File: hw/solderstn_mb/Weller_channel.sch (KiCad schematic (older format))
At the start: 40 parts, among them U1401 AD8552ARU, U1402 INA226, U1403 TPS2HB16AQ1, U1404 INA226, U1405 74LVC1G11, U1406 74LVC1G11, U1407 74LVC1G11

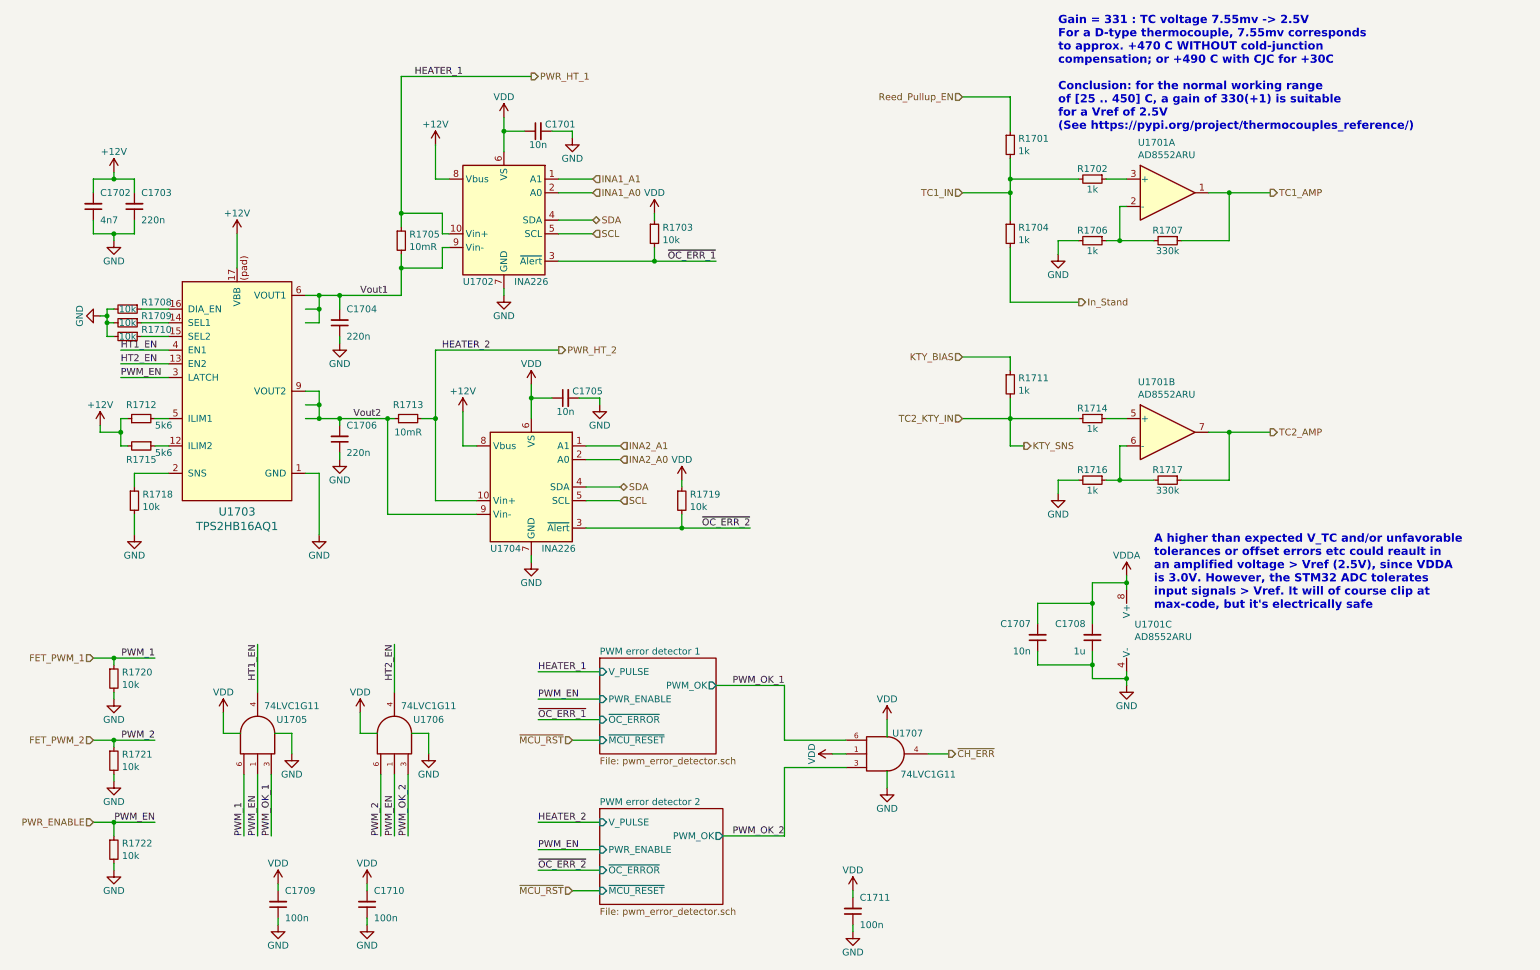
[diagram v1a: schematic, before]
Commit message: * Remove separate REED_PULLUP_EN pin; instead bias the Reedswitches with the per-channel KTY bias (buffered Vref) * Add separate mini cut-out sub-PCB for 3.5 headphone connector at back-panel (must be angled vertical to fit in panel) * Some ESD and buffering on back panel
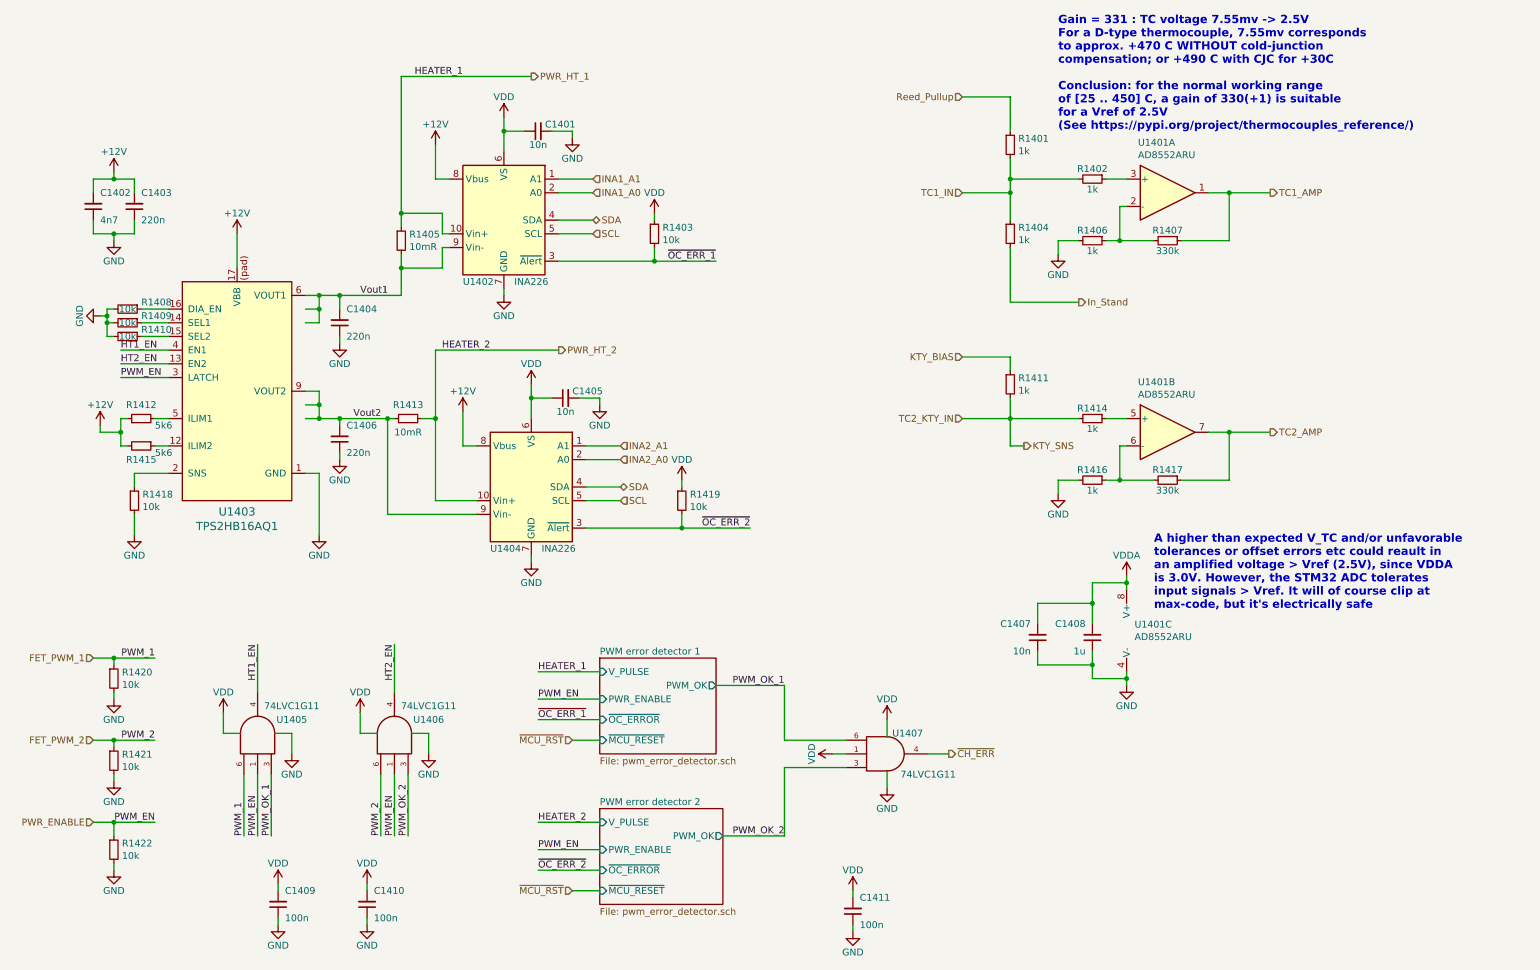
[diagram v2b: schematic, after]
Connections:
- net Reed_Pullup_EN renamed Reed_Pullup

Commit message: Updated display-board sch & PCB with optional left-hand rotary encoder instead of pwrbtn. Printed MB schematic updates PDF for 20-08-21
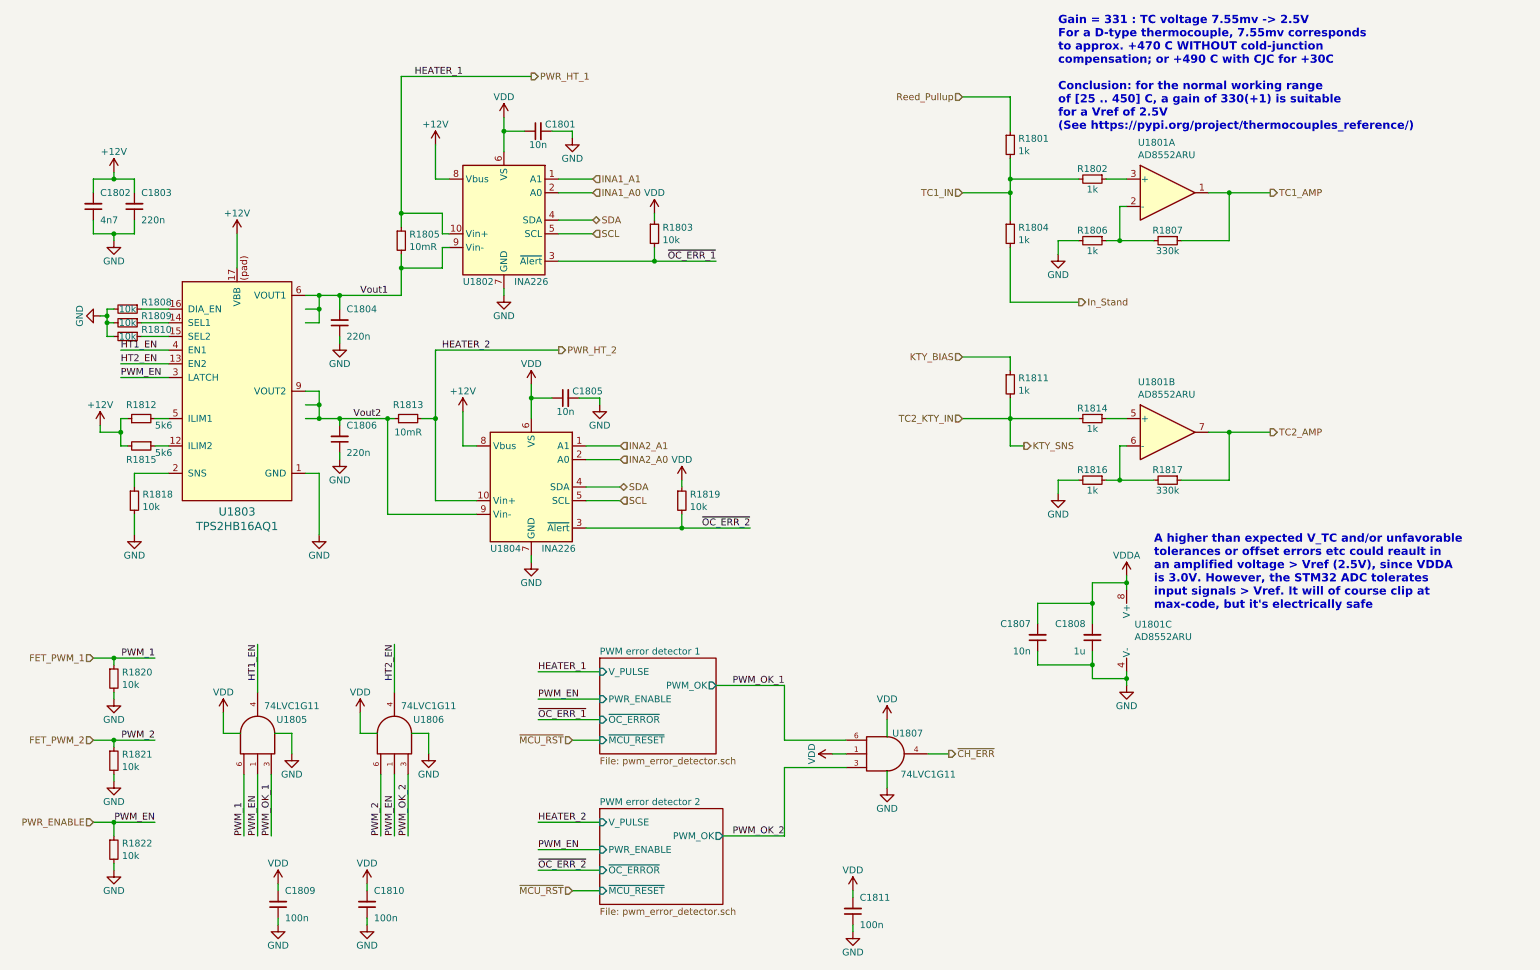
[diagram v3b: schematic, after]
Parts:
- renumbered C1401 to C1501, C1402 to C1502, C1403 to C1503, C1404 to C1504, C1405 to C1505, C1406 to C1506, C1407 to C1507, C1408 to C1508, C1409 to C1509, C1410 to C1510, C1411 to C1511, R1401 to R1501, R1402 to R1502, R1403 to R1503, R1404 to R1504, R1405 to R1505, R1406 to R1506, R1407 to R1507, R1408 to R1508, R1409 to R1509, R1410 to R1510, R1411 to R1511, R1412 to R1512, R1413 to R1513, R1414 to R1514, R1415 to R1515, R1416 to R1516, R1417 to R1517, R1418 to R1518, R1419 to R1519, R1420 to R1520, R1421 to R1521, R1422 to R1522, U1401 to U1501, U1402 to U1502, U1403 to U1503, U1404 to U1504, U1405 to U1505, U1406 to U1506, U1407 to U1507

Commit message: Corrected several ERC issues. Re-annotated & assigned all footprints except 32k xtal (will prob. replace with RTC module anyway)
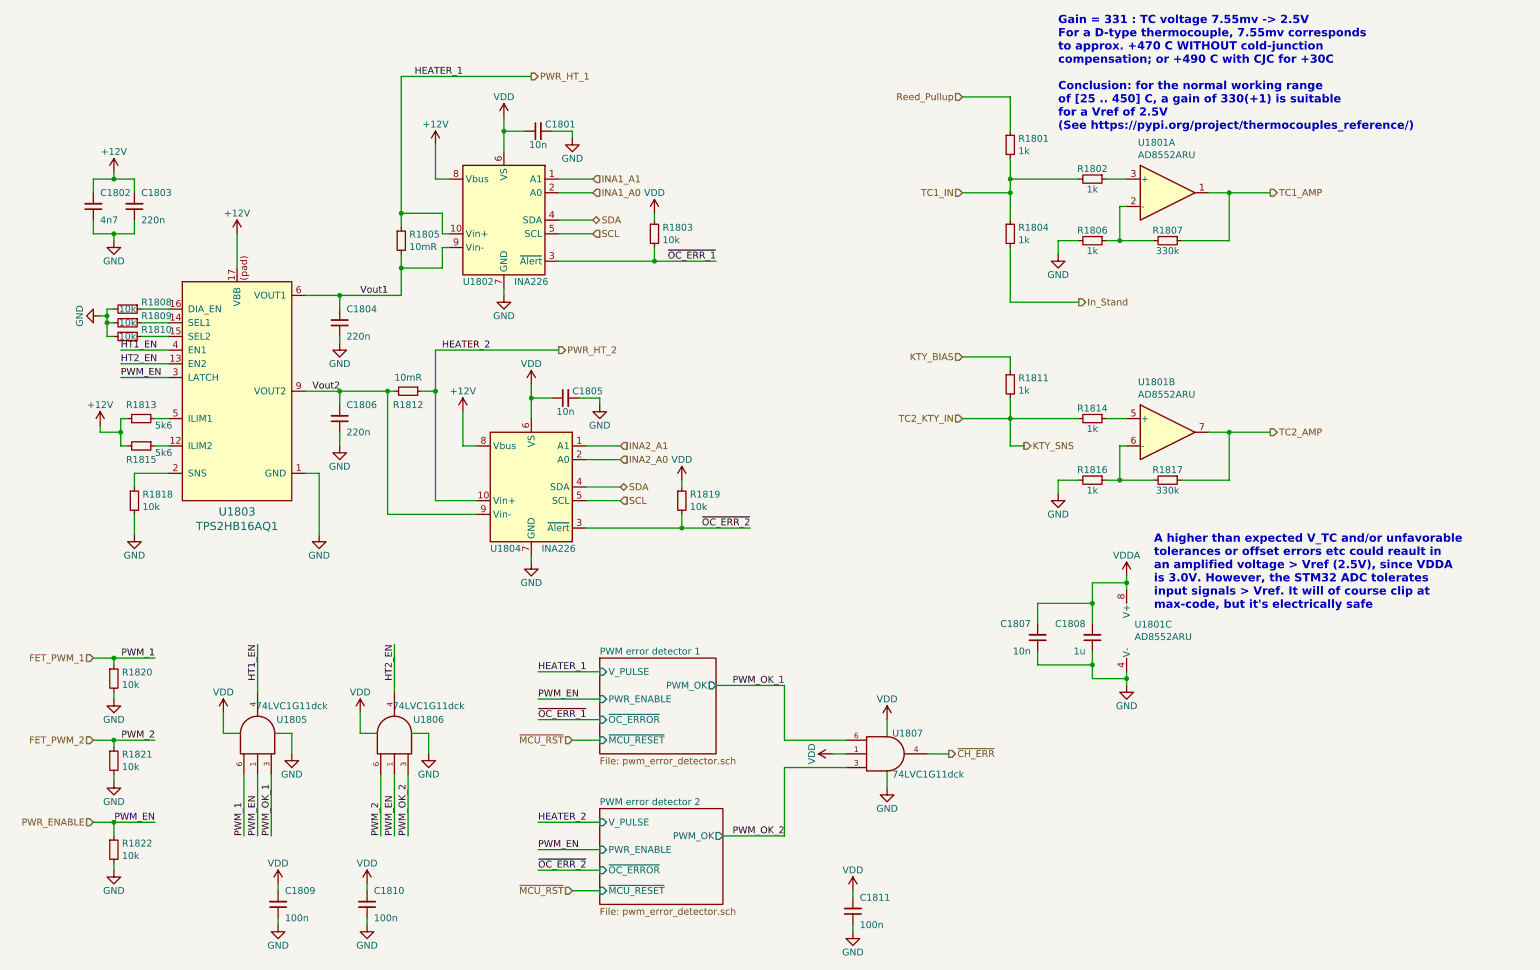
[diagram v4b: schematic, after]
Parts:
- C1501, C1502, C1503, C1504, C1505, C1506, C1507, C1508, C1509, C1510, C1511: footprint (none) -> Capacitor_SMD:C_0603_1608Metric
- R1501, R1502, R1503, R1504, R1506, R1507, R1508, R1509, R1510, R1511, R1514, R1515, R1516, R1517, R1518, R1519, R1520, R1521, R1522: footprint (none) -> Resistor_SMD:R_0603_1608Metric
- R1513: renamed from R1512; footprint (none) -> Resistor_SMD:R_0603_1608Metric
- U1505, U1506, U1507: value 74LVC1G11 -> 74LVC1G11dck; footprint (none) -> Package_TO_SOT_SMD:SOT-363_SC-70-6_Handsoldering
- renumbered R1513 to R1512
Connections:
- net PWR_HT_2: now also R1512.1; no longer R1512.2
- net Vout2: now also R1512.2; no longer R1512.1
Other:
- moved on the sheet: C1806, R1812
